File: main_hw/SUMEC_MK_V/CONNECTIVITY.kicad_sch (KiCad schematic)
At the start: 22 parts, among them J4 USB_TypeC, U5 USBLC6-2SC6

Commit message: plotting + boms
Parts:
- F1: value Polyfuse/50R -> Polyfuse/0R
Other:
- moved on the sheet: D5, D6, D7, D8, R23, R24, R25, R30

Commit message: 67yfhtgftu
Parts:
- renumbered D8 to D7, D7 to D8, R21 to R18, R22 to R19, R18 to R20, R23 to R21, R24 to R22, R19 to R23, R20 to R24, R30 to R25, R25 to R26, R26 to R27
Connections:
- net BZ_PWM renamed BZ_IO02
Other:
- moved on the sheet: D5, D6, R21, R22

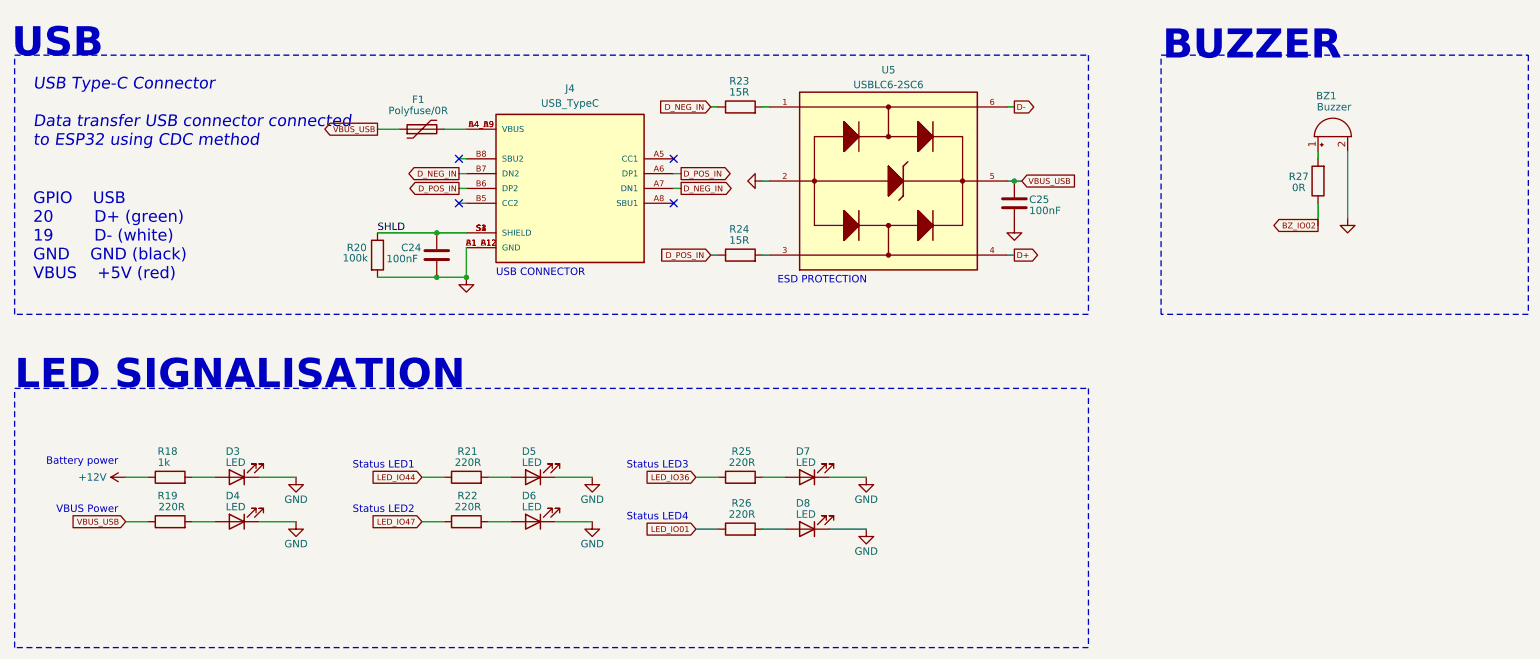
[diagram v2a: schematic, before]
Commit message: MK5 bugfix fixed POL_L, minor changes, deleted nSLEEP and nFault connections to the MCU
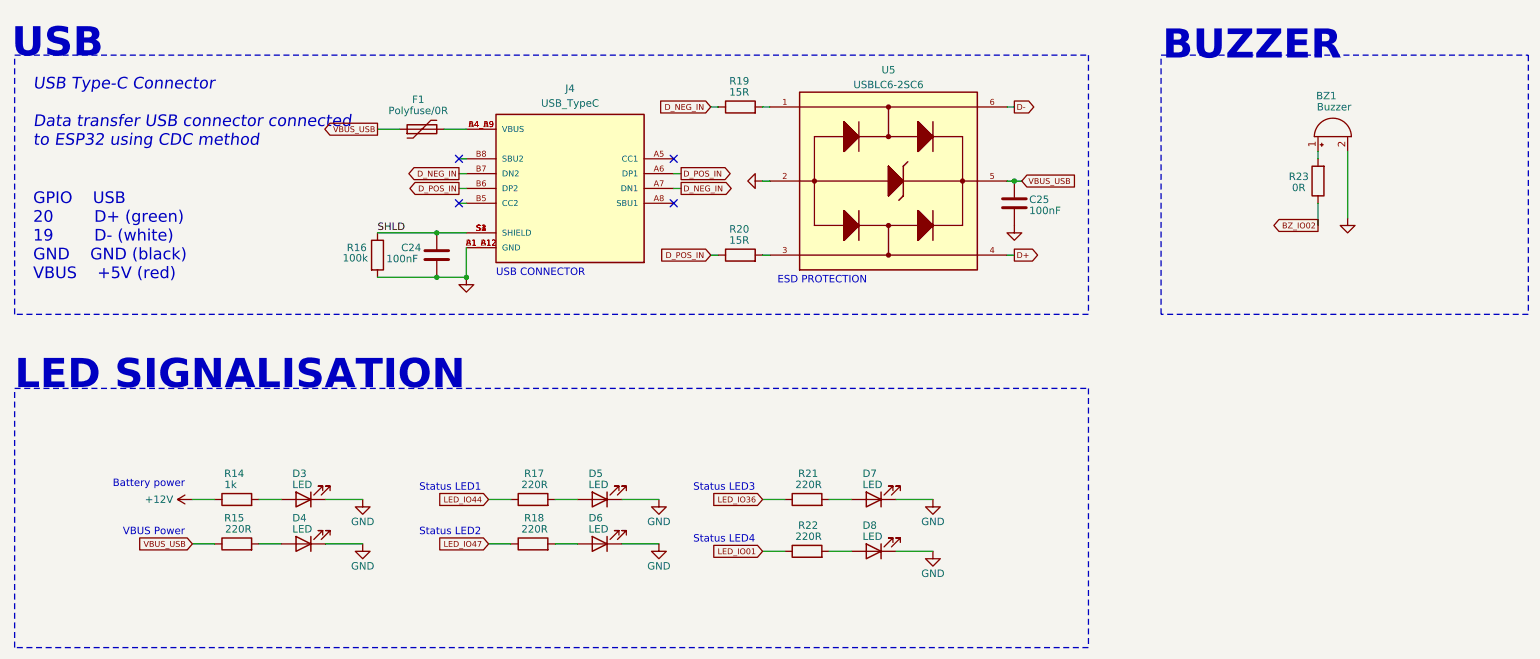
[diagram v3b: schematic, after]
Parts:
- renumbered R18 to R14, R19 to R15, R20 to R16, R21 to R17, R22 to R18, R23 to R19, R24 to R20, R25 to R21, R26 to R22, R27 to R23
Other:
- moved on the sheet: D3, D4, D5, D6, D7, D8, R14, R15, R17, R18, R21, R22

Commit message: updates to mk5
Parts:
- renumbered C24 to C23, C25 to C24, D3 to D4, D4 to D5, D5 to D6, D6 to D7, D7 to D8, D8 to D9, R14 to R13, R15 to R14, R16 to R15, R17 to R16, R18 to R17, R19 to R18, R20 to R19, R21 to R20, R22 to R21, R23 to R22
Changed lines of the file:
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@@
 		(on_board yes)
 		(dnp no)
-		(property "Reference" "#PWR067"
+		(property "Reference" "#PWR064"
 			(at 127 115.57 0)
 			(effects
@@
 			(project "SUMEC_MK_V"
 				(path "/900bd7ac-cdf9-4a2f-8b1f-2c21e3760046/ce2ae977-07a3-41c1-b3e1-68b5a1d5517b"
-					(reference "#PWR067")
+					(reference "#PWR064")
 					(unit 1)
 				)
@@
 		(on_board yes)
 		(dnp no)
-		(property "Reference" "R22"
+		(property "Reference" "R21"
 			(at 154.305 106.045 90)
 			(effects
@@
 			(project "SUMEC_MK_V"
 				(path "/900bd7ac-cdf9-4a2f-8b1f-2c21e3760046/ce2ae977-07a3-41c1-b3e1-68b5a1d5517b"
-					(reference "R22")
+					(reference "R21")
 					(unit 1)
 				)
@@
 		(on_board yes)
 		(dnp no)
-		(property "Reference" "D7"
+		(property "Reference" "D8"
 			(at 161.925 97.155 0)
 			(effects
@@
 			(project "SUMEC_MK_V"
 				(path "/900bd7ac-cdf9-4a2f-8b1f-2c21e3760046/ce2ae977-07a3-41c1-b3e1-68b5a1d5517b"
-					(reference "D7")
+					(reference "D8")
 					(unit 1)
 				)
@@
 		(on_board yes)
 		(dnp no)
-		(property "Reference" "R14"
+		(property "Reference" "R13"
 			(at 55.88 97.155 90)
 			(effects
@@
 			(project "SUMEC_MK_V"
 				(path "/900bd7ac-cdf9-4a2f-8b1f-2c21e3760046/ce2ae977-07a3-41c1-b3e1-68b5a1d5517b"
-					(reference "R14")
+					(reference "R13")
 					(unit 1)
 				)
@@
 		(on_board yes)
 		(dnp no)
-		(property "Reference" "#PWR063"
+		(property "Reference" "#PWR060"
 			(at 76.2 107.95 0)
 			(effects
@@
 			(project "SUMEC_MK_V"
 				(path "/900bd7ac-cdf9-4a2f-8b1f-2c21e3760046/ce2ae977-07a3-41c1-b3e1-68b5a1d5517b"
-					(reference "#PWR063")
+					(reference "#PWR060")
 					(unit 1)
 				)
@@
 		(on_board yes)
 		(dnp no)
-		(property "Reference" "R15"
+		(property "Reference" "R14"
 			(at 55.88 104.775 90)
 			(effects
@@
 			(project "SUMEC_MK_V"
 				(path "/900bd7ac-cdf9-4a2f-8b1f-2c21e3760046/ce2ae977-07a3-41c1-b3e1-68b5a1d5517b"
-					(reference "R15")
+					(reference "R14")
 					(unit 1)
 				)
@@
 		(dnp no)
 		(fields_autoplaced yes)
-		(property "Reference" "#PWR068"
+		(property "Reference" "#PWR065"
 			(at 138.43 46.99 0)
 			(effects
@@
 			(project "SUMEC_MK_V"
 				(path "/900bd7ac-cdf9-4a2f-8b1f-2c21e3760046/ce2ae977-07a3-41c1-b3e1-68b5a1d5517b"
-					(reference "#PWR068")
+					(reference "#PWR065")
 					(unit 1)
 				)
@@
 		(on_board yes)
 		(dnp no)
-		(property "Reference" "#PWR064"
+		(property "Reference" "#PWR061"
 			(at 76.2 115.57 0)
 			(effects
@@
 			(project "SUMEC_MK_V"
 				(path "/900bd7ac-cdf9-4a2f-8b1f-2c21e3760046/ce2ae977-07a3-41c1-b3e1-68b5a1d5517b"
-					(reference "#PWR064")
+					(reference "#PWR061")
 					(unit 1)
 				)
@@
 		(dnp no)
 		(fields_autoplaced yes)
-		(property "Reference" "#PWR072"
+		(property "Reference" "#PWR069"
 			(at 245.11 59.69 0)
 			(effects
@@
 			(project "SUMEC_MK_V"
 				(path "/900bd7ac-cdf9-4a2f-8b1f-2c21e3760046/ce2ae977-07a3-41c1-b3e1-68b5a1d5517b"
-					(reference "#PWR072")
+					(reference "#PWR069")
 					(unit 1)
 				)
@@
 		(on_board yes)
 		(dnp no)
-		(property "Reference" "R17"
+		(property "Reference" "R16"
 			(at 107.315 97.155 90)
 			(effects
@@
 			(project "SUMEC_MK_V"
 				(path "/900bd7ac-cdf9-4a2f-8b1f-2c21e3760046/ce2ae977-07a3-41c1-b3e1-68b5a1d5517b"
-					(reference "R17")
+					(reference "R16")
 					(unit 1)
 				)
@@
 		(on_board yes)
 		(dnp no)
-		(property "Reference" "#PWR070"
+		(property "Reference" "#PWR067"
 			(at 173.99 116.84 0)
 			(effects
@@
 			(project "SUMEC_MK_V"
 				(path "/900bd7ac-cdf9-4a2f-8b1f-2c21e3760046/ce2ae977-07a3-41c1-b3e1-68b5a1d5517b"
-					(reference "#PWR070")
+					(reference "#PWR067")
 					(unit 1)
 				)
@@
 		(on_board yes)
 		(dnp no)
-		(property "Reference" "R19"
+		(property "Reference" "R18"
 			(at 139.065 29.845 90)
 			(effects
@@
 			(project "SUMEC_MK_V"
 				(path "/900bd7ac-cdf9-4a2f-8b1f-2c21e3760046/ce2ae977-07a3-41c1-b3e1-68b5a1d5517b"
-					(reference "R19")
+					(reference "R18")
 					(unit 1)
 				)
@@
 		(dnp no)
 		(fields_autoplaced yes)
-		(property "Reference" "#PWR065"
+		(property "Reference" "#PWR062"
 			(at 93.98 69.85 0)
 			(effects
@@
 			(project "SUMEC_MK_V"
 				(path "/900bd7ac-cdf9-4a2f-8b1f-2c21e3760046/ce2ae977-07a3-41c1-b3e1-68b5a1d5517b"
-					(reference "#PWR065")
+					(reference "#PWR062")
 					(unit 1)
 				)
@@
 		(on_board yes)
 		(dnp no)
-		(property "Reference" "R20"
+		(property "Reference" "R19"
 			(at 139.065 55.245 90)
 			(effects
@@
 			(project "SUMEC_MK_V"
 				(path "/900bd7ac-cdf9-4a2f-8b1f-2c21e3760046/ce2ae977-07a3-41c1-b3e1-68b5a1d5517b"
-					(reference "R20")
+					(reference "R19")
 					(unit 1)
 				)
@@
 		(dnp no)
 		(fields_autoplaced yes)
-		(property "Reference" "#PWR071"
+		(property "Reference" "#PWR068"
 			(at 187.96 60.96 0)
 			(effects
@@
 			(project "SUMEC_MK_V"
 				(path "/900bd7ac-cdf9-4a2f-8b1f-2c21e3760046/ce2ae977-07a3-41c1-b3e1-68b5a1d5517b"
-					(reference "#PWR071")
+					(reference "#PWR068")
 					(unit 1)
 				)
@@
 		(on_board yes)
 		(dnp no)
-		(property "Reference" "#PWR069"
+		(property "Reference" "#PWR066"
 			(at 173.99 107.95 0)
 			(effects
@@
 			(project "SUMEC_MK_V"
 				(path "/900bd7ac-cdf9-4a2f-8b1f-2c21e3760046/ce2ae977-07a3-41c1-b3e1-68b5a1d5517b"
-					(reference "#PWR069")
+					(reference "#PWR066")
 					(unit 1)
 				)
@@
 		(on_board yes)
 		(dnp no)
-		(property "Reference" "D3"
+		(property "Reference" "D4"
 			(at 64.135 97.155 0)
 			(effects
@@
 			(project "SUMEC_MK_V"
 				(path "/900bd7ac-cdf9-4a2f-8b1f-2c21e3760046/ce2ae977-07a3-41c1-b3e1-68b5a1d5517b"
-					(reference "D3")
+					(reference "D4")
 					(unit 1)
 				)
@@
 		(on_board yes)
 		(dnp no)
-		(property "Reference" "#PWR062"
+		(property "Reference" "#PWR059"
 			(at 50.8 101.6 0)
 			(effects
@@
 			(project "SUMEC_MK_V"
 				(path "/900bd7ac-cdf9-4a2f-8b1f-2c21e3760046/ce2ae977-07a3-41c1-b3e1-68b5a1d5517b"
-					(reference "#PWR062")
+					(reference "#PWR059")
 					(unit 1)
 				)
@@
 		(on_board yes)
 		(dnp no)
-		(property "Reference" "D8"
+		(property "Reference" "D9"
 			(at 161.925 106.045 0)
 			(effects
@@
 			(project "SUMEC_MK_V"
 				(path "/900bd7ac-cdf9-4a2f-8b1f-2c21e3760046/ce2ae977-07a3-41c1-b3e1-68b5a1d5517b"
-					(reference "D8")
+					(reference "D9")
 					(unit 1)
 				)
@@
 		(on_board yes)
 		(dnp no)
-		(property "Reference" "C25"
+		(property "Reference" "C24"
 			(at 190.5 50.165 0)
 			(effects
@@
 			(project "SUMEC_MK_V"
 				(path "/900bd7ac-cdf9-4a2f-8b1f-2c21e3760046/ce2ae977-07a3-41c1-b3e1-68b5a1d5517b"
-					(reference "C25")
+					(reference "C24")
 					(unit 1)
 				)
@@
 		(on_board yes)
 		(dnp no)
-		(property "Reference" "C24"
+		(property "Reference" "C23"
 			(at 82.804 58.42 0)
 			(effects
@@
 			(project "SUMEC_MK_V"
 				(path "/900bd7ac-cdf9-4a2f-8b1f-2c21e3760046/ce2ae977-07a3-41c1-b3e1-68b5a1d5517b"
-					(reference "C24")
+					(reference "C23")
 					(unit 1)
 				)
@@
 		(on_board yes)
 		(dnp no)
-		(property "Reference" "D5"
+		(property "Reference" "D6"
 			(at 114.935 97.155 0)
 			(effects
@@
 			(project "SUMEC_MK_V"
 				(path "/900bd7ac-cdf9-4a2f-8b1f-2c21e3760046/ce2ae977-07a3-41c1-b3e1-68b5a1d5517b"
-					(reference "D5")
+					(reference "D6")
 					(unit 1)
 				)
@@
 		(on_board yes)
 		(dnp no)
-		(property "Reference" "#PWR066"
+		(property "Reference" "#PWR063"
 			(at 127 107.95 0)
 			(effects
@@
 			(project "SUMEC_MK_V"
 				(path "/900bd7ac-cdf9-4a2f-8b1f-2c21e3760046/ce2ae977-07a3-41c1-b3e1-68b5a1d5517b"
-					(reference "#PWR066")
+					(reference "#PWR063")
 					(unit 1)
 				)
@@
 		(on_board yes)
 		(dnp no)
-		(property "Reference" "R21"
+		(property "Reference" "R20"
 			(at 154.305 97.155 90)
 			(effects
@@
 			(project "SUMEC_MK_V"
 				(path "/900bd7ac-cdf9-4a2f-8b1f-2c21e3760046/ce2ae977-07a3-41c1-b3e1-68b5a1d5517b"
-					(reference "R21")
+					(reference "R20")
 					(unit 1)
 				)
@@
 		(on_board yes)
 		(dnp no)
-		(property "Reference" "D4"
+		(property "Reference" "D5"
 			(at 64.135 104.775 0)
 			(effects
@@
 			(project "SUMEC_MK_V"
 				(path "/900bd7ac-cdf9-4a2f-8b1f-2c21e3760046/ce2ae977-07a3-41c1-b3e1-68b5a1d5517b"
-					(reference "D4")
+					(reference "D5")
 					(unit 1)
 				)
@@
 		(on_board yes)
 		(dnp no)
-		(property "Reference" "R16"
+		(property "Reference" "R15"
 			(at 75.184 58.42 0)
 			(effects
@@
 			(project "SUMEC_MK_V"
 				(path "/900bd7ac-cdf9-4a2f-8b1f-2c21e3760046/ce2ae977-07a3-41c1-b3e1-68b5a1d5517b"
-					(reference "R16")
+					(reference "R15")
 					(unit 1)
 				)
@@
 		(on_board yes)
 		(dnp no)
-		(property "Reference" "D6"
+		(property "Reference" "D7"
 			(at 114.935 104.775 0)
 			(effects
@@
 			(project "SUMEC_MK_V"
 				(path "/900bd7ac-cdf9-4a2f-8b1f-2c21e3760046/ce2ae977-07a3-41c1-b3e1-68b5a1d5517b"
-					(reference "D6")
+					(reference "D7")
 					(unit 1)
 				)
@@
 		(on_board yes)
 		(dnp no)
-		(property "Reference" "R23"
+		(property "Reference" "R22"
 			(at 236.728 46.228 0)
 			(effects
@@
 			(project "SUMEC_MK_V"
 				(path "/900bd7ac-cdf9-4a2f-8b1f-2c21e3760046/ce2ae977-07a3-41c1-b3e1-68b5a1d5517b"
-					(reference "R23")
+					(reference "R22")
 					(unit 1)
 				)
@@
 		(on_board yes)
 		(dnp no)
-		(property "Reference" "R18"
+		(property "Reference" "R17"
 			(at 107.315 104.775 90)
 			(effects
@@
 			(project "SUMEC_MK_V"
 				(path "/900bd7ac-cdf9-4a2f-8b1f-2c21e3760046/ce2ae977-07a3-41c1-b3e1-68b5a1d5517b"
-					(reference "R18")
-					(unit 1)
-				)
+					(reference "R17")
+					(unit 1)
+				)

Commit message: MK5 PCB rework
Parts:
- removed BZ1: Buzzer, Schrack_brd:BUZZER_CUI_CPT, symbol Device:Buzzer
- removed C23, C24: 100nF, Capacitor_SMD:C_0805_2012Metric_Pad1.18x1.45mm_HandSolder, symbol Device:C
- removed D4, D5, D6, D7, D8, D9: LED, LED_SMD:LED_0805_2012Metric_Pad1.15x1.40mm_HandSolder, symbol Device:LED
- removed F1: Polyfuse/0R, Fuse:Fuse_0805_2012Metric, symbol Device:Polyfuse
- removed J4: USB_TypeC, sumec_brd:HRO_TYPE-C-31-M-12, symbol sumec_sch_lib:USB_TypeC
- removed R13: 1k, Resistor_SMD:R_0805_2012Metric_Pad1.20x1.40mm_HandSolder, symbol Device:R
- removed R14, R16, R17, R20, R21: 220R, Resistor_SMD:R_0805_2012Metric_Pad1.20x1.40mm_HandSolder, symbol Device:R
- removed R15: 100k, Resistor_SMD:R_0805_2012Metric_Pad1.20x1.40mm_HandSolder, symbol Device:R
- removed R18, R19: 15R, Resistor_SMD:R_0805_2012Metric_Pad1.20x1.40mm_HandSolder, symbol Device:R
- removed R22: 0R, Resistor_SMD:R_0805_2012Metric_Pad1.20x1.40mm_HandSolder, symbol Device:R
- removed U5: USBLC6-2SC6, Package_TO_SOT_SMD:TSOT-23-6_HandSoldering, symbol sumec_library:USBLC6-2SC6
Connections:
- no-connect marks 4 -> 0
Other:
- note removed: "BUZZER"
- note removed: "Battery power"
- note removed: "ESD PROTECTION"
- note removed: "GPIO USB 20 D+ (green) 19 D- (white) GND GND (black) VBUS +5V (red)"
- note removed: "LED SIGNALISATION"
- note removed: "Status LED1"
- note removed: "Status LED2"
- note removed: "Status LED3"
- note removed: "Status LED4"
- note removed: "USB"
- note removed: "USB CONNECTOR"
- note removed: "USB Type-C Connector Data transfer USB connector connected to ESP32 using CDC method"
- note removed: "VBUS Power"
